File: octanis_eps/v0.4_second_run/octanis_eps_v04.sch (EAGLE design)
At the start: 104 parts, among them IC1 OPA2333DGK, IC5 OPA2333DGK, IC7 OPA2333DGK, IC9 OPA2333DGK, Q1 FC-12M, Q2 N-HEXFET-2D_SOT232-, Q3 N-HEXFET-2D_SOT232-, Q4 N-HEXFET-2D_SOT232-

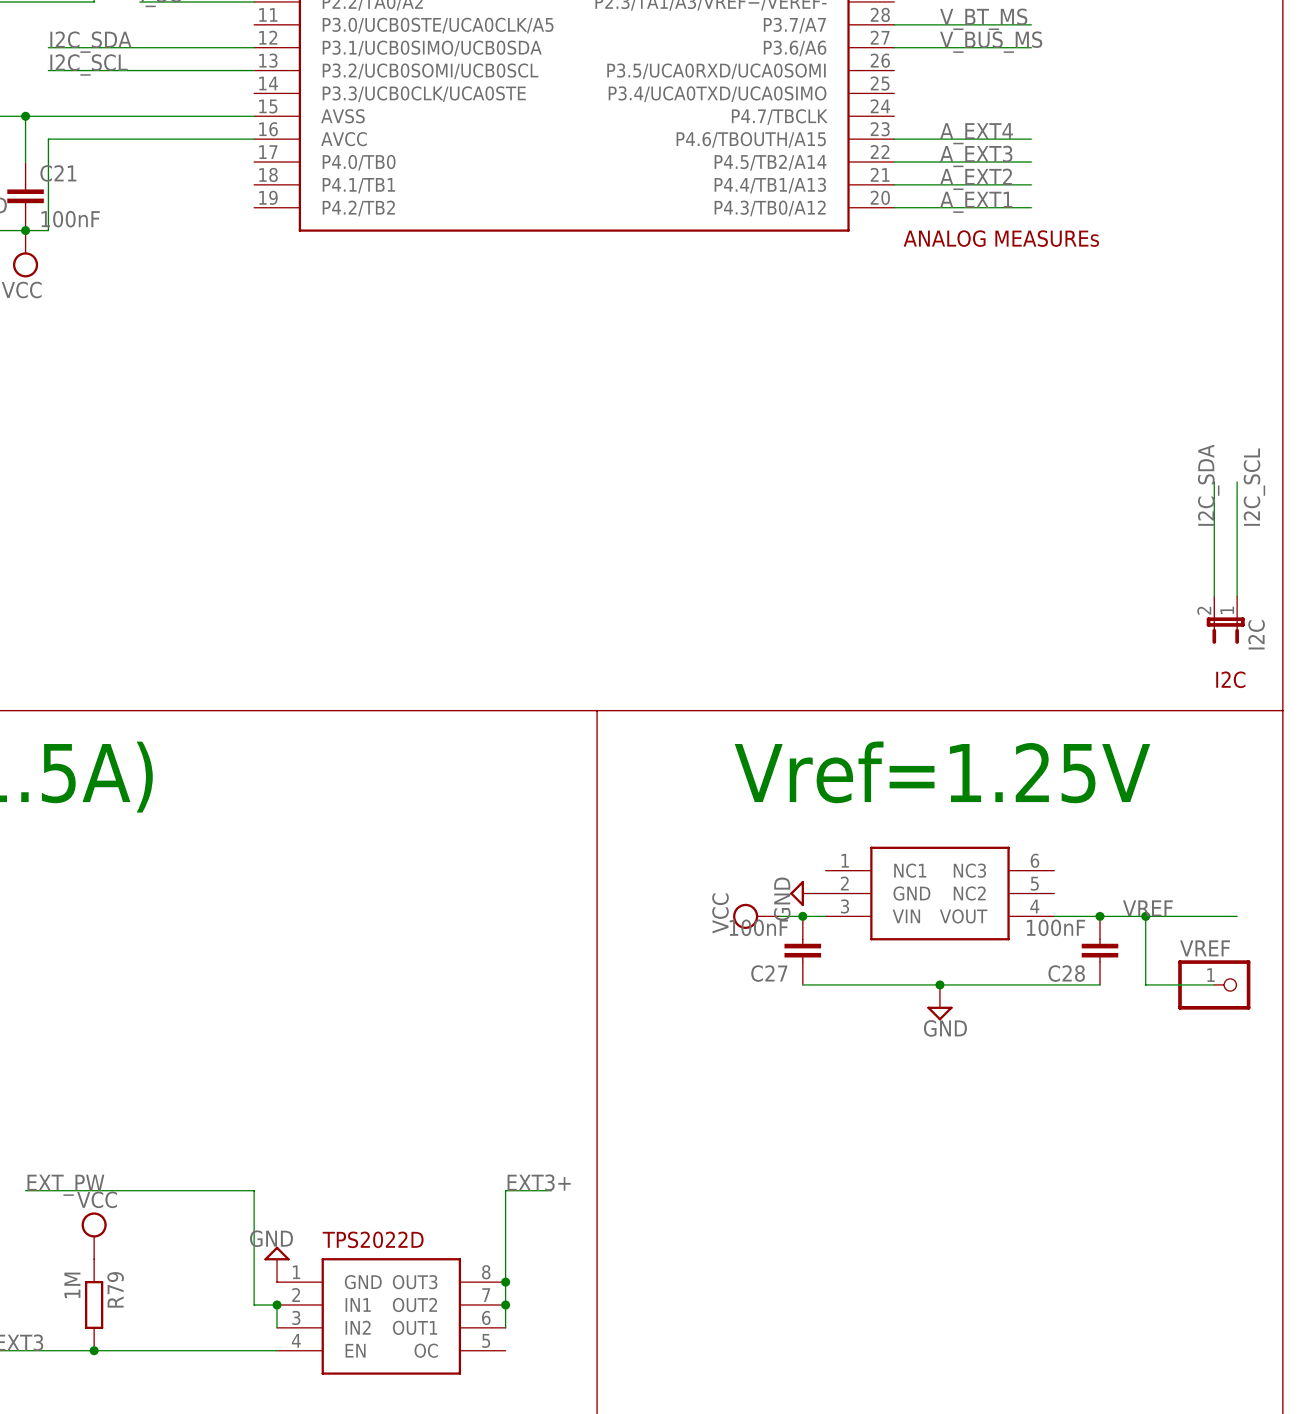
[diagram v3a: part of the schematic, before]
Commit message: changed ADR127 1.25V ref for MAX6190BESA (lower power), added 2 pins with pull down for main board sleep, DRC checked. One OPA2333 need to be changed on disispation circuit.
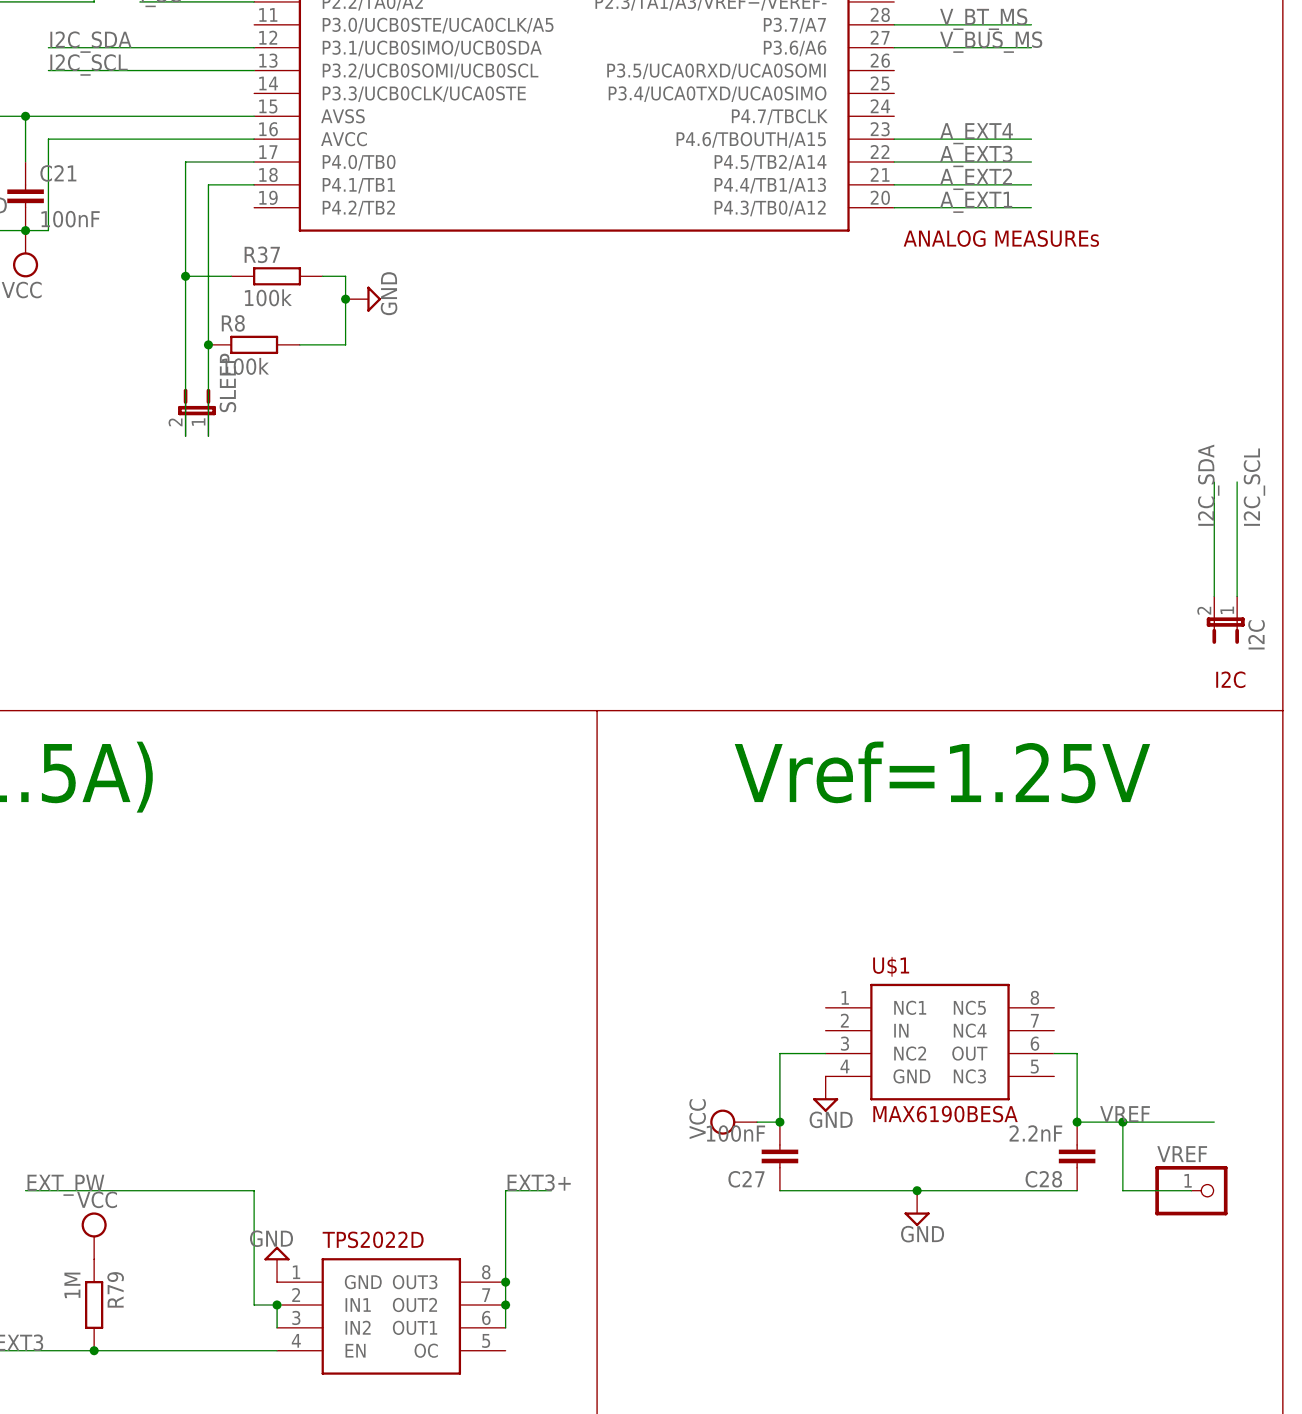
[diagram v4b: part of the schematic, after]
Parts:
- removed U$19: ADR127B, Octanis1_EPS:ADR127B
- added R37, R8: 100k, rcl:R-EU_R0603
- added SLEEP: (no value), jumper:JP1E
- added U$1: MAX6190BESA, Octanis1_EPS:MAX6190BESA
- C28: value 100nF -> 2.2nF
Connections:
- new net N$27: R8.1, SLEEP.1, U$6.P4.1/TB1
- new net N$36: R37.1, SLEEP.2, U$6.P4.0/TB0
- net GND: now also R37.2, R8.2, U$1.GND; no longer U$19.GND
- net VCC: now also U$1.NC2; no longer U$19.VIN
- net VREF: now also U$1.OUT; no longer U$19.VOUT
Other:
- moved on the sheet: C27, C28, VREF
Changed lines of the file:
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@@
 <part name="SUPPLY124" library="supply2" deviceset="VCC" device=""/>
 <part name="SUPPLY125" library="supply2" deviceset="VCC" device=""/>
-<part name="U$19" library="Octanis1_EPS" deviceset="ADR127B" device=""/>
 <part name="C27" library="rcl" deviceset="C-EU" device="C0603" value="100nF"/>
-<part name="C28" library="rcl" deviceset="C-EU" device="C0603" value="100nF"/>
+<part name="C28" library="rcl" deviceset="C-EU" device="C0603" value="2.2nF"/>
 <part name="SUPPLY118" library="supply2" deviceset="GND" device=""/>
 <part name="SUPPLY126" library="supply2" deviceset="VCC" device=""/>
@@
 <part name="R6" library="rcl" deviceset="R-EU_" device="R0603" value="100k"/>
 <part name="SUPPLY59" library="supply2" deviceset="GND" device=""/>
+<part name="SLEEP" library="jumper" deviceset="JP1E" device=""/>
+<part name="U$1" library="Octanis1_EPS" deviceset="MAX6190BESA" device=""/>
+<part name="R8" library="rcl" deviceset="R-EU_" device="R0603" value="100k"/>
+<part name="R37" library="rcl" deviceset="R-EU_" device="R0603" value="100k"/>
+<part name="SUPPLY60" library="supply2" deviceset="GND" device=""/>
 </parts>
 <sheets>
@@
 <instance part="SUPPLY124" gate="G$1" x="233.68" y="-78.74"/>
 <instance part="SUPPLY125" gate="G$1" x="312.42" y="-114.3"/>
-<instance part="U$19" gate="G$1" x="406.4" y="-76.2"/>
-<instance part="C27" gate="G$1" x="391.16" y="-83.82" rot="R180"/>
-<instance part="C28" gate="G$1" x="424.18" y="-83.82" rot="R180"/>
-<instance part="SUPPLY118" gate="GND" x="391.16" y="-76.2" rot="R270"/>
-<instance part="SUPPLY126" gate="G$1" x="386.08" y="-78.74" rot="R90"/>
-<instance part="SUPPLY128" gate="GND" x="406.4" y="-88.9"/>
+<instance part="C27" gate="G$1" x="388.62" y="-106.68" rot="R180"/>
+<instance part="C28" gate="G$1" x="421.64" y="-106.68" rot="R180"/>
+<instance part="SUPPLY118" gate="GND" x="393.7" y="-99.06"/>
+<instance part="SUPPLY126" gate="G$1" x="383.54" y="-101.6" rot="R90"/>
+<instance part="SUPPLY128" gate="GND" x="403.86" y="-111.76"/>
 <instance part="R10" gate="G$1" x="114.3" y="-198.12" rot="R270"/>
 <instance part="R11" gate="G$1" x="177.8" y="-182.88" rot="R180"/>
@@
 <instance part="SUPPLY50" gate="G$1" x="66.04" y="-193.04"/>
 <instance part="SUPPLY51" gate="GND" x="66.04" y="-210.82"/>
-<instance part="VREF" gate="G$1" x="439.42" y="-86.36"/>
+<instance part="VREF" gate="G$1" x="436.88" y="-109.22"/>
 <instance part="VCC" gate="G$1" x="289.56" y="-12.7" rot="R270"/>
 <instance part="R42" gate="G$1" x="-33.02" y="58.42" rot="R270"/>
@@
 <instance part="R6" gate="G$1" x="101.6" y="-182.88" rot="R270"/>
 <instance part="SUPPLY59" gate="GND" x="101.6" y="-190.5"/>
+<instance part="SLEEP" gate="A" x="325.12" y="-22.86" rot="MR0"/>
+<instance part="U$1" gate="G$1" x="406.4" y="-91.44"/>
+<instance part="R8" gate="G$1" x="330.2" y="-15.24"/>
+<instance part="R37" gate="G$1" x="332.74" y="-7.62"/>
+<instance part="SUPPLY60" gate="GND" x="342.9" y="-10.16" rot="R90"/>
 </instances>
 <busses>
@@
 </segment>
 <segment>
-<pinref part="U$19" gate="G$1" pin="GND"/>
-<pinref part="SUPPLY118" gate="GND" pin="GND"/>
-</segment>
-<segment>
 <pinref part="C27" gate="G$1" pin="1"/>
 <pinref part="C28" gate="G$1" pin="1"/>
-<wire x1="391.16" y1="-86.36" x2="406.4" y2="-86.36" width="0.1524" layer="91"/>
+<wire x1="388.62" y1="-109.22" x2="403.86" y2="-109.22" width="0.1524" layer="91"/>
 <pinref part="SUPPLY128" gate="GND" pin="GND"/>
-<wire x1="406.4" y1="-86.36" x2="424.18" y2="-86.36" width="0.1524" layer="91"/>
-<junction x="406.4" y="-86.36"/>
+<wire x1="403.86" y1="-109.22" x2="421.64" y2="-109.22" width="0.1524" layer="91"/>
+<junction x="403.86" y="-109.22"/>
 </segment>
 <segment>
@@
 <pinref part="SUPPLY59" gate="GND" pin="GND"/>
 </segment>
+<segment>
+<pinref part="U$1" gate="G$1" pin="GND"/>
+<pinref part="SUPPLY118" gate="GND" pin="GND"/>
+</segment>
+<segment>
+<pinref part="R37" gate="G$1" pin="2"/>
+<wire x1="337.82" y1="-7.62" x2="340.36" y2="-7.62" width="0.1524" layer="91"/>
+<pinref part="SUPPLY60" gate="GND" pin="GND"/>
+<wire x1="340.36" y1="-7.62" x2="340.36" y2="-10.16" width="0.1524" layer="91"/>
+<wire x1="340.36" y1="-10.16" x2="340.36" y2="-15.24" width="0.1524" layer="91"/>
+<junction x="340.36" y="-10.16"/>
+<pinref part="R8" gate="G$1" pin="2"/>
+<wire x1="340.36" y1="-15.24" x2="335.28" y2="-15.24" width="0.1524" layer="91"/>
+</segment>
 </net>
 <net name="VCC" class="0">
@@
 </segment>
 <segment>
-<pinref part="U$19" gate="G$1" pin="VIN"/>
 <pinref part="SUPPLY126" gate="G$1" pin="VCC"/>
-<wire x1="388.62" y1="-78.74" x2="391.16" y2="-78.74" width="0.1524" layer="91"/>
+<wire x1="386.08" y1="-101.6" x2="388.62" y2="-101.6" width="0.1524" layer="91"/>
 <pinref part="C27" gate="G$1" pin="2"/>
-<wire x1="391.16" y1="-78.74" x2="393.7" y2="-78.74" width="0.1524" layer="91"/>
-<junction x="391.16" y="-78.74"/>
+<wire x1="388.62" y1="-101.6" x2="388.62" y2="-93.98" width="0.1524" layer="91"/>
+<junction x="388.62" y="-101.6"/>
+<pinref part="U$1" gate="G$1" pin="NC2"/>
+<wire x1="388.62" y1="-93.98" x2="393.7" y2="-93.98" width="0.1524" layer="91"/>
 </segment>
 <segment>
@@
 </segment>
 <segment>
-<pinref part="U$19" gate="G$1" pin="VOUT"/>
 <pinref part="C28" gate="G$1" pin="2"/>
-<wire x1="419.1" y1="-78.74" x2="424.18" y2="-78.74" width="0.1524" layer="91"/>
-<wire x1="424.18" y1="-78.74" x2="429.26" y2="-78.74" width="0.1524" layer="91"/>
-<junction x="424.18" y="-78.74"/>
-<label x="426.72" y="-78.74" size="1.778" layer="95"/>
-<wire x1="429.26" y1="-78.74" x2="429.26" y2="-86.36" width="0.1524" layer="91"/>
+<wire x1="421.64" y1="-101.6" x2="426.72" y2="-101.6" width="0.1524" layer="91"/>
+<junction x="421.64" y="-101.6"/>
+<label x="424.18" y="-101.6" size="1.778" layer="95"/>
+<wire x1="426.72" y1="-101.6" x2="426.72" y2="-109.22" width="0.1524" layer="91"/>
 <pinref part="VREF" gate="G$1" pin="1"/>
-<wire x1="429.26" y1="-86.36" x2="436.88" y2="-86.36" width="0.1524" layer="91"/>
-<wire x1="429.26" y1="-78.74" x2="439.42" y2="-78.74" width="0.1524" layer="91"/>
-<junction x="429.26" y="-78.74"/>
+<wire x1="426.72" y1="-109.22" x2="434.34" y2="-109.22" width="0.1524" layer="91"/>
+<wire x1="426.72" y1="-101.6" x2="436.88" y2="-101.6" width="0.1524" layer="91"/>
+<junction x="426.72" y="-101.6"/>
+<pinref part="U$1" gate="G$1" pin="OUT"/>
+<wire x1="419.1" y1="-93.98" x2="421.64" y2="-93.98" width="0.1524" layer="91"/>
+<wire x1="421.64" y1="-93.98" x2="421.64" y2="-101.6" width="0.1524" layer="91"/>
 </segment>
 <segment>
@@
 </segment>
 </net>
+<net name="N$27" class="0">
+<segment>
+<pinref part="U$6" gate="G$1" pin="P4.1/TB1"/>
+<wire x1="330.2" y1="2.54" x2="325.12" y2="2.54" width="0.1524" layer="91"/>
+<wire x1="325.12" y1="2.54" x2="325.12" y2="-15.24" width="0.1524" layer="91"/>
+<pinref part="R8" gate="G$1" pin="1"/>
+<pinref part="SLEEP" gate="A" pin="1"/>
+<wire x1="325.12" y1="-15.24" x2="325.12" y2="-25.4" width="0.1524" layer="91"/>
+<junction x="325.12" y="-15.24"/>
+</segment>
+</net>
+<net name="N$36" class="0">
+<segment>
+<pinref part="U$6" gate="G$1" pin="P4.0/TB0"/>
+<wire x1="330.2" y1="5.08" x2="322.58" y2="5.08" width="0.1524" layer="91"/>
+<pinref part="R37" gate="G$1" pin="1"/>
+<wire x1="322.58" y1="-7.62" x2="322.58" y2="5.08" width="0.1524" layer="91"/>
+<wire x1="327.66" y1="-7.62" x2="322.58" y2="-7.62" width="0.1524" layer="91"/>
+<pinref part="SLEEP" gate="A" pin="2"/>
+<wire x1="322.58" y1="-7.62" x2="322.58" y2="-25.4" width="0.1524" layer="91"/>
+<junction x="322.58" y="-7.62"/>
+</segment>
+</net>
